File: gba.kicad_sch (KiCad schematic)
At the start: 30 parts, among them IC1 STM32MP157AAB3, IC10 HSP051-4M10, IC7 S40FC004C1B2C00000, IC9 HSP051-4M10, J2 Conn_01x02, J3 MEM2075-00-140-01-A, SW1 SW_MEC_5G, SW2 SW_MEC_5G

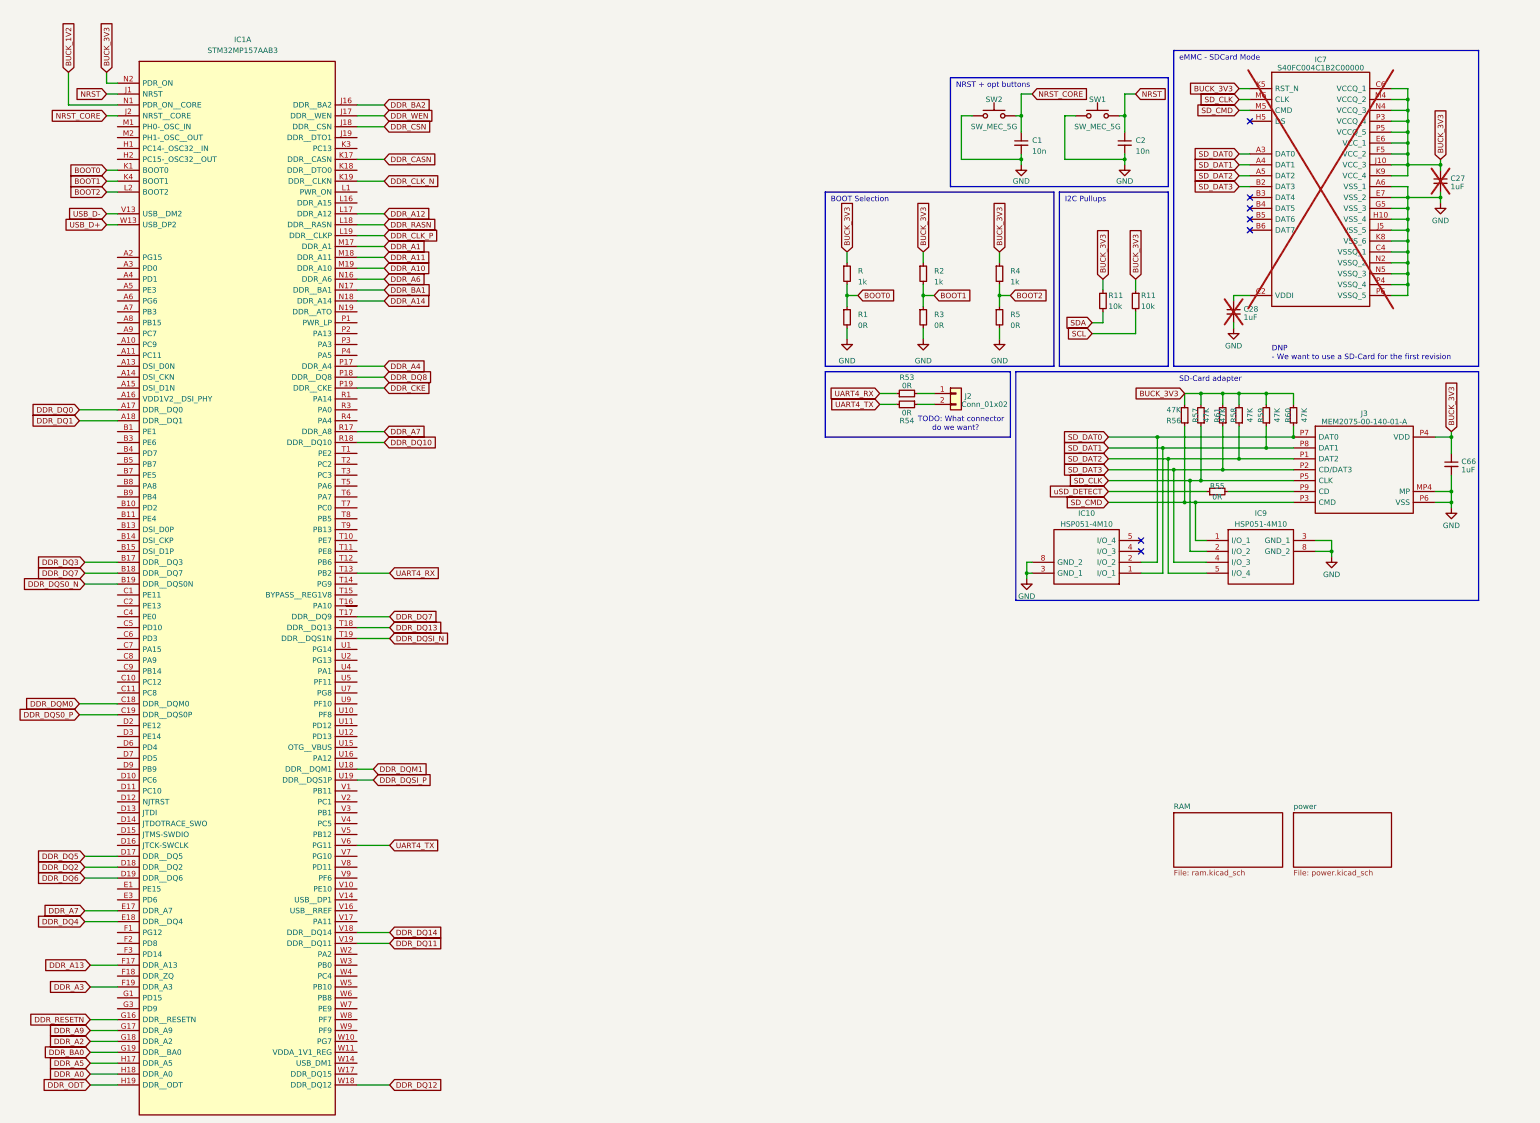
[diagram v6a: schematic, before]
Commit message: Add level shifter for uSD
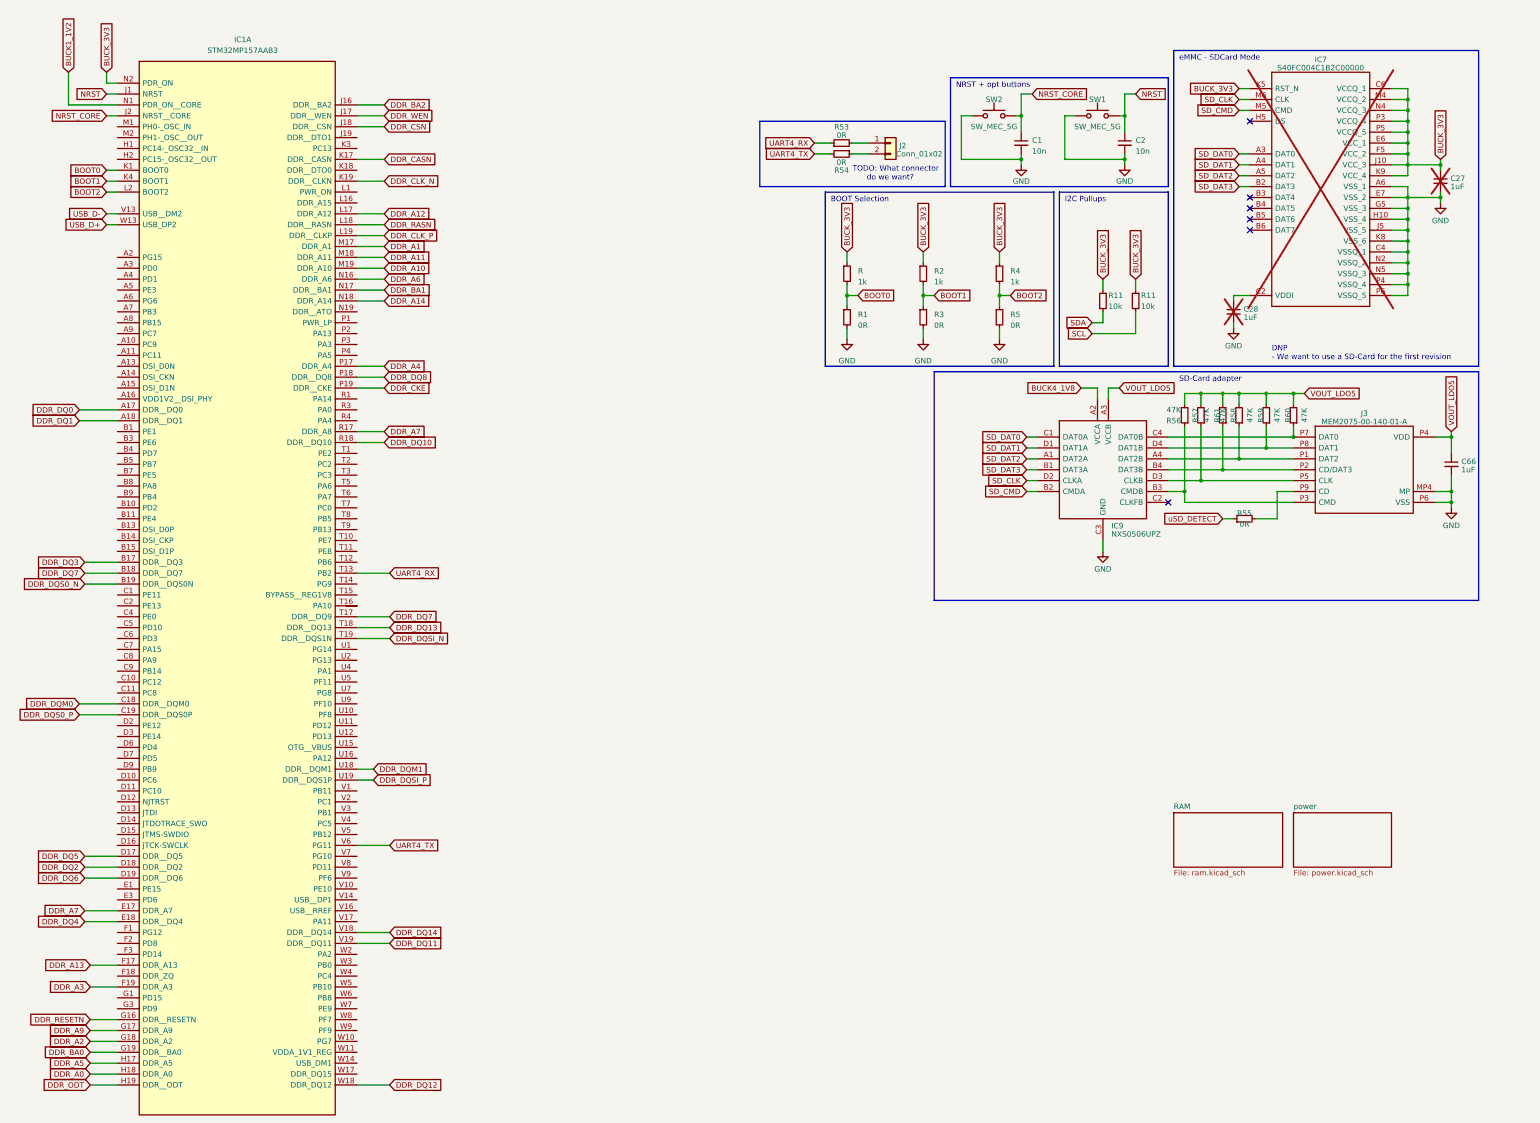
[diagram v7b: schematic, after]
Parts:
- removed IC10, IC9: HSP051-4M10, HSP0514M10, symbol ARMband:HSP051-4M10
- added IC9: NXS0506UPZ, BGA16C35P4X4_146X146X47, symbol ARMband:NXS0506UPZ
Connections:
- net BUCK_3V3: no longer C66.1, J3.P4 (VDD), R56.2, R57.2, R58.2, R59.2, R60.2, R61.2
- net GND: now also IC9.C3 (GND)
- net SD_CLK: now also IC9.D2 (CLKA); no longer J3.P5 (CLK), R57.1
- net SD_CMD: now also IC9.B2 (CMDA); no longer J3.P3 (CMD), R56.1
- net SD_DAT0: now also IC9.C1 (DAT0A); no longer J3.P7 (DAT0), R60.1
- net SD_DAT1: now also IC9.D1 (DAT1A); no longer J3.P8 (DAT1), R59.1
- net SD_DAT2: now also IC9.A1 (DAT2A); no longer J3.P1 (DAT2), R58.1
- net SD_DAT3: now also IC9.B1 (DAT3A); no longer J3.P2 (CD/DAT3), R61.1
- net BUCK_1V2 renamed BUCK1_1V2
- new net: IC9.B3 (CMDB), J3.P3 (CMD), R56.1
- new net: IC9.A4 (DAT2B), J3.P1 (DAT2), R58.1
- new net: IC9.B4 (DAT3B), J3.P2 (CD/DAT3), R61.1
- new net: IC9.C4 (DAT0B), J3.P7 (DAT0), R60.1
- new net: IC9.D3 (CLKB), J3.P5 (CLK), R57.1
- new net: IC9.D4 (DAT1B), J3.P8 (DAT1), R59.1
- new net BUCK4_1V8: IC9.A2 (VCCA)
- new net VOUT_LDO5: C66.1, IC9.A3 (VCCB), J3.P4 (VDD), R56.2, R57.2, R58.2, R59.2, R60.2, R61.2
- no-connect marks 7 -> 6
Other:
- moved on the sheet: J2, R53, R54, R55

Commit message: 3v3 to 1V8 rework
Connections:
- net BUCK4_1V8: now also C27.1, IC1.N2 (PDR_ON), IC7.C6 (VCCQ_1), IC7.E6 (VCC_1), IC7.F5 (VCC_2), IC7.J10 (VCC_3), IC7.K9 (VCC_4), IC7.M4 (VCCQ_2), IC7.N4 (VCCQ_3), IC7.P3 (VCCQ_4), IC7.P5 (VCCQ_5), R.1, R11.1, R11.1, R2.1, R4.1
- net BUCK_3V3: no longer C27.1, IC1.N2 (PDR_ON), IC7.C6 (VCCQ_1), IC7.E6 (VCC_1), IC7.F5 (VCC_2), IC7.J10 (VCC_3), IC7.K9 (VCC_4), IC7.M4 (VCCQ_2), IC7.N4 (VCCQ_3), IC7.P3 (VCCQ_4), IC7.P5 (VCCQ_5), R.1, R11.1, R11.1, R2.1, R4.1
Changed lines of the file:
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@@
     )
   )
-  (global_label "BUCK_3V3" (shape input) (at 271.78 72.39 90) (fields_autoplaced)
+  (global_label "BUCK4_1V8" (shape input) (at 271.78 72.39 90) (fields_autoplaced)
     (effects (font (size 1.27 1.27)) (justify left))
     (property "Intersheetrefs" "${INTERSHEET_REFS}" (at 271.78 65.9766 90)
@@
     )
   )
-  (global_label "BUCK_3V3" (shape input) (at 81.28 30.48 90) (fields_autoplaced)
+  (global_label "BUCK4_1V8" (shape input) (at 81.28 30.48 90) (fields_autoplaced)
     (effects (font (size 1.27 1.27)) (justify left))
     (property "Intersheetrefs" "${INTERSHEET_REFS}" (at 81.28 24.0666 90)
@@
     )
   )
-  (global_label "BUCK_3V3" (shape input) (at 321.31 78.74 90) (fields_autoplaced)
+  (global_label "BUCK4_1V8" (shape input) (at 321.31 78.74 90) (fields_autoplaced)
     (effects (font (size 1.27 1.27)) (justify left))
     (property "Intersheetrefs" "${INTERSHEET_REFS}" (at 321.31 66.2185 90)
@@
     )
   )
-  (global_label "BUCK_3V3" (shape input) (at 392.43 50.8 90) (fields_autoplaced)
+  (global_label "BUCK4_1V8" (shape input) (at 392.43 50.8 90) (fields_autoplaced)
     (effects (font (size 1.27 1.27)) (justify left))
     (property "Intersheetrefs" "${INTERSHEET_REFS}" (at 392.43 38.2785 90)
@@
     )
   )
-  (global_label "BUCK_3V3" (shape input) (at 313.69 78.74 90) (fields_autoplaced)
+  (global_label "BUCK4_1V8" (shape input) (at 313.69 78.74 90) (fields_autoplaced)
     (effects (font (size 1.27 1.27)) (justify left))
     (property "Intersheetrefs" "${INTERSHEET_REFS}" (at 313.69 66.2185 90)
@@
     )
   )
-  (global_label "BUCK_3V3" (shape input) (at 289.56 72.39 90) (fields_autoplaced)
+  (global_label "BUCK4_1V8" (shape input) (at 289.56 72.39 90) (fields_autoplaced)
     (effects (font (size 1.27 1.27)) (justify left))
     (property "Intersheetrefs" "${INTERSHEET_REFS}" (at 289.56 65.9766 90)
@@
     )
   )
-  (global_label "BUCK_3V3" (shape input) (at 254 72.39 90) (fields_autoplaced)
+  (global_label "BUCK4_1V8" (shape input) (at 254 72.39 90) (fields_autoplaced)
     (effects (font (size 1.27 1.27)) (justify left))
     (property "Intersheetrefs" "${INTERSHEET_REFS}" (at 254 65.9766 90)
